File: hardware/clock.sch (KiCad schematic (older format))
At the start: 64 parts, among them U301 ADCMP580, U302 CDCLVP1204, U303 SY89321L-synth_lib, U304 ICS853S057I, U305 X0060L5050AHF, X301 DV75D-010.0M

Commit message: first pass of layout complete
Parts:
- U303: footprint Housings_DFN_QFN:DFN-8-1EP_2x2mm_Pitch0.5mm -> vna_footprints:DFN-8-1EP_2x2mm_Pitch0.5mm
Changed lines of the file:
@@
 F 0 "U303" H 11800 4265 50  0000 C CNN
 F 1 "SY89321L-synth_lib" H 11800 4174 50  0000 C CNN
-F 2 "Housings_DFN_QFN:DFN-8-1EP_2x2mm_Pitch0.5mm" H 11700 3850 50  0001 C CNN
+F 2 "vna_footprints:DFN-8-1EP_2x2mm_Pitch0.5mm" H 11700 3850 50  0001 C CNN
 F 3 "" H 11700 3850 50  0001 C CNN
 	1    11800 3850

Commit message: fixed CML termination.. ready to order?
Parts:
- C308, C309: value .01 uF -> 10 nF
- R309, R311: value 125 -> 50
- R310, R312: value 84 -> DNP
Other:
- note removed: "TODO:VERIFY PECL/LVPECL COMPATIBILITY"
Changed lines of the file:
@@
 AR Path="/5BC3F72A/5BE80179" Ref="C309"  Part="1"
 F 0 "C309" H 9292 8946 50  0000 L CNN
-F 1 ".01 uF" H 9292 8855 50  0000 L CNN
+F 1 "10 nF" H 9292 8855 50  0000 L CNN
 F 2 "Capacitors_SMD:C_0402" H 9200 8900 50  0001 C CNN
 F 3 "~" H 9200 8900 50  0001 C CNN
@@
 AR Path="/5BC3F72A/5BEB36FF" Ref="C308"  Part="1"
 F 0 "C308" H 9292 8346 50  0000 L CNN
-F 1 ".01 uF" H 9292 8255 50  0000 L CNN
+F 1 "10 nF" H 9292 8255 50  0000 L CNN
 F 2 "Capacitors_SMD:C_0402" H 9200 8300 50  0001 C CNN
 F 3 "~" H 9200 8300 50  0001 C CNN
@@
 AR Path="/5BC3F72A/5C014D4A" Ref="R310"  Part="1"
 F 0 "R310" H 7650 7200 50  0000 C CNN
-F 1 "84" H 7650 7100 50  0000 C CNN
+F 1 "DNP" H 7650 7100 50  0000 C CNN
 F 2 "Resistors_SMD:R_0402" H 7500 7150 50  0001 C CNN
 F 3 "~" H 7500 7150 50  0001 C CNN
@@
 AR Path="/5BC3F72A/5C014E27" Ref="R312"  Part="1"
 F 0 "R312" H 8000 7200 50  0000 C CNN
-F 1 "84" H 8000 7100 50  0000 C CNN
+F 1 "DNP" H 8000 7100 50  0000 C CNN
 F 2 "Resistors_SMD:R_0402" H 7850 7150 50  0001 C CNN
 F 3 "~" H 7850 7150 50  0001 C CNN
@@
 AR Path="/5BC3F72A/5C014F03" Ref="R309"  Part="1"
 F 0 "R309" H 7650 6550 50  0000 C CNN
-F 1 "125" H 7650 6450 50  0000 C CNN
+F 1 "50" H 7650 6450 50  0000 C CNN
 F 2 "Resistors_SMD:R_0402" H 7500 6500 50  0001 C CNN
 F 3 "~" H 7500 6500 50  0001 C CNN
@@
 AR Path="/5BC3F72A/5C014FD6" Ref="R311"  Part="1"
 F 0 "R311" H 8000 6550 50  0000 C CNN
-F 1 "125" H 8000 6450 50  0000 C CNN
+F 1 "50" H 8000 6450 50  0000 C CNN
 F 2 "Resistors_SMD:R_0402" H 7850 6500 50  0001 C CNN
 F 3 "~" H 7850 6500 50  0001 C CNN
@@
 	1    0    0    1
 $EndComp
-Text Notes 4450 6650 0    50   ~ 10
-TODO:VERIFY PECL/LVPECL COMPATIBILITY
-$Comp
-L power:GND #PWR?
+$Comp
+L power:GND #PWR?

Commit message: schematic cleanup, BOM consolidation
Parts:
- C322, C324, C325: value 2.2 uF -> 4.7 uF
- R304: value TBD -> 1k
- R306: value R_Small -> JMP
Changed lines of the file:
@@
 P 5750 4150
 F 0 "R306" V 5946 4150 50  0000 C CNN
-F 1 "R_Small" V 5855 4150 50  0000 C CNN
+F 1 "JMP" V 5855 4150 50  0000 C CNN
 F 2 "Resistors_SMD:R_0402" H 5750 4150 50  0001 C CNN
 F 3 "~" H 5750 4150 50  0001 C CNN
@@
 AR Path="/5BC3F72A/5BF5E71F" Ref="R304"  Part="1"
 F 0 "R304" V 3200 5850 50  0000 L CNN
-F 1 "TBD" V 3200 5650 50  0000 L CNN
+F 1 "1k" V 3200 5650 50  0000 L CNN
 F 2 "Resistors_SMD:R_0402" H 3300 5800 50  0001 C CNN
 F 3 "~" H 3300 5800 50  0001 C CNN
@@
 P 4550 5850
 F 0 "C324" H 4642 5896 50  0000 L CNN
-F 1 "2.2 uF" H 4600 5750 50  0000 L CNN
+F 1 "4.7 uF" H 4600 5750 50  0000 L CNN
 F 2 "Capacitors_SMD:C_0603" H 4550 5850 50  0001 C CNN
 F 3 "~" H 4550 5850 50  0001 C CNN
@@
 P 2050 5850
 F 0 "C322" H 2142 5896 50  0000 L CNN
-F 1 "2.2 uF" H 2100 5750 50  0000 L CNN
+F 1 "4.7 uF" H 2100 5750 50  0000 L CNN
 F 2 "Capacitors_SMD:C_0603" H 2050 5850 50  0001 C CNN
 F 3 "~" H 2050 5850 50  0001 C CNN
@@
 P 14050 5500
 F 0 "C325" H 14142 5546 50  0000 L CNN
-F 1 "2.2 uF" H 14100 5400 50  0000 L CNN
+F 1 "4.7 uF" H 14100 5400 50  0000 L CNN
 F 2 "Capacitors_SMD:C_0603" H 14050 5500 50  0001 C CNN
 F 3 "~" H 14050 5500 50  0001 C CNN

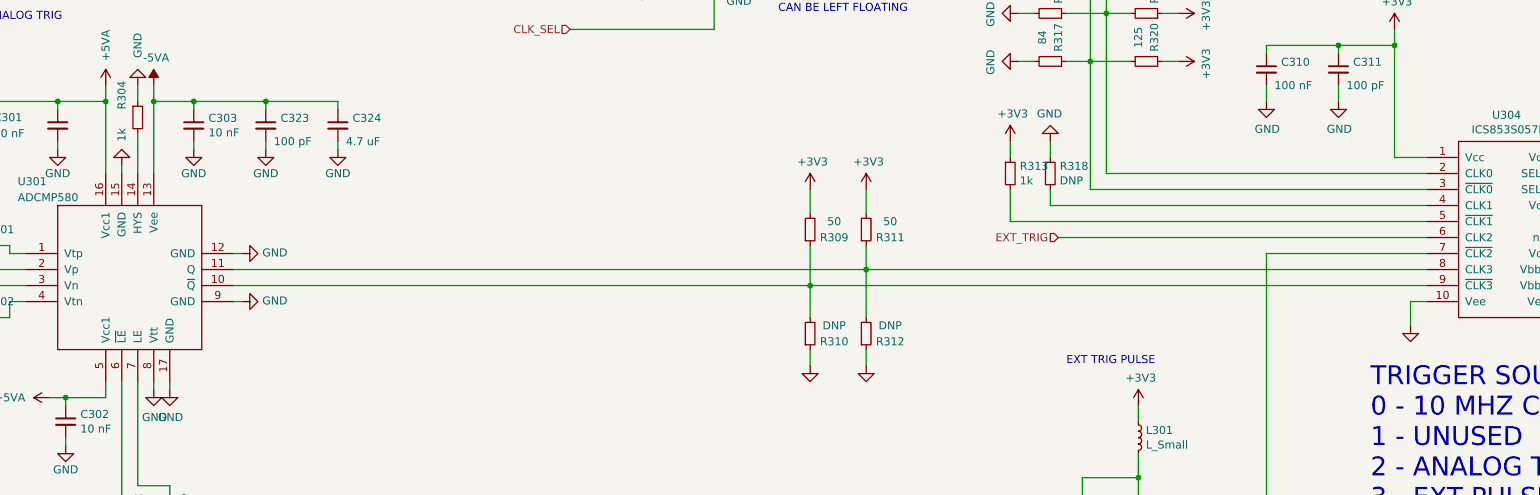
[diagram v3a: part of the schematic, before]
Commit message: fix crossover distortion on analog triggered measurements
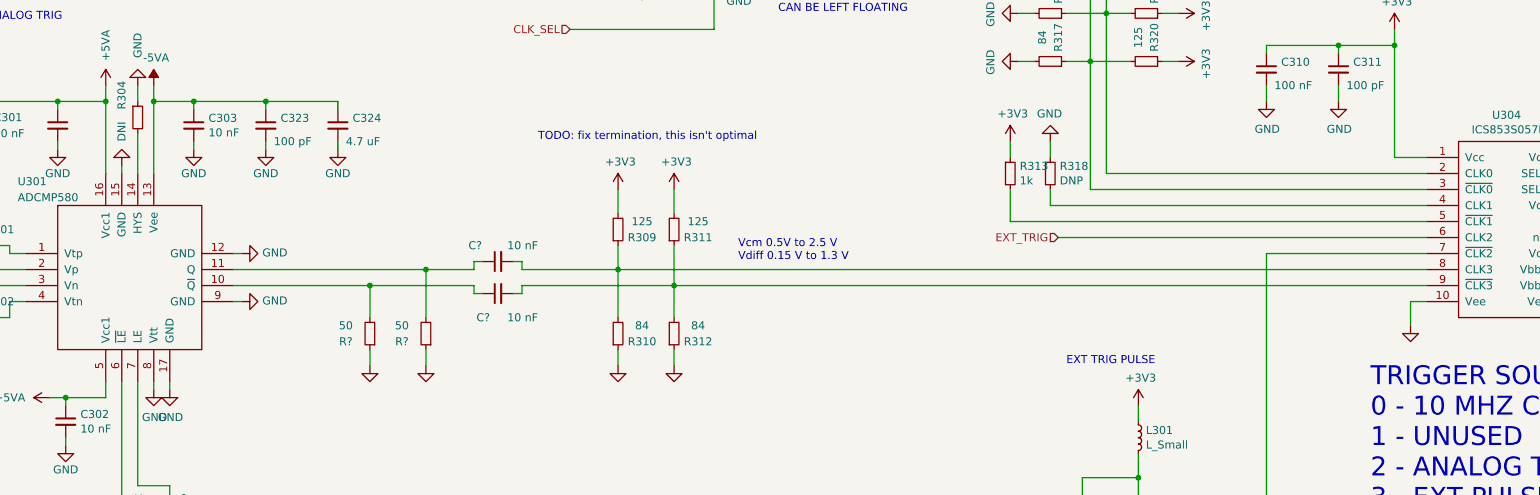
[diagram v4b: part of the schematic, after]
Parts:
- added C? (x2): 10 nF, Capacitors_SMD:C_0402, symbol Device:C_Small
- added R? (x2): 50, Resistors_SMD:R_0402, symbol Device:R_Small
- R304: value 1k -> DNI
- R309, R311: value 50 -> 125
- R310, R312: value DNP -> 84
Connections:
- net GND: now also R?.1, R?.1
- net at R311.1, R312.2: now also U304.9 (~CLK3), C?.2; no longer U301.11 (Q), U304.8 (CLK3)
- net at R309.1, R310.2: now also U304.8 (CLK3), C?.2; no longer U301.10 (~Q), U304.9 (~CLK3)
- new net: C?.1, R?.2, U301.10 (~Q)
- new net: C?.1, R?.2, U301.11 (Q)
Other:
- note added: "TODO: fix termination, this isn't optimal"
- note added: "Vcm 0.5V to 2.5 V\nVdiff 0.15 V to 1.3 V"
- moved on the sheet: R309, R310, R311, R312
